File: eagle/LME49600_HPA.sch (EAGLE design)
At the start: 20 parts, among them IC1 OPA2134P

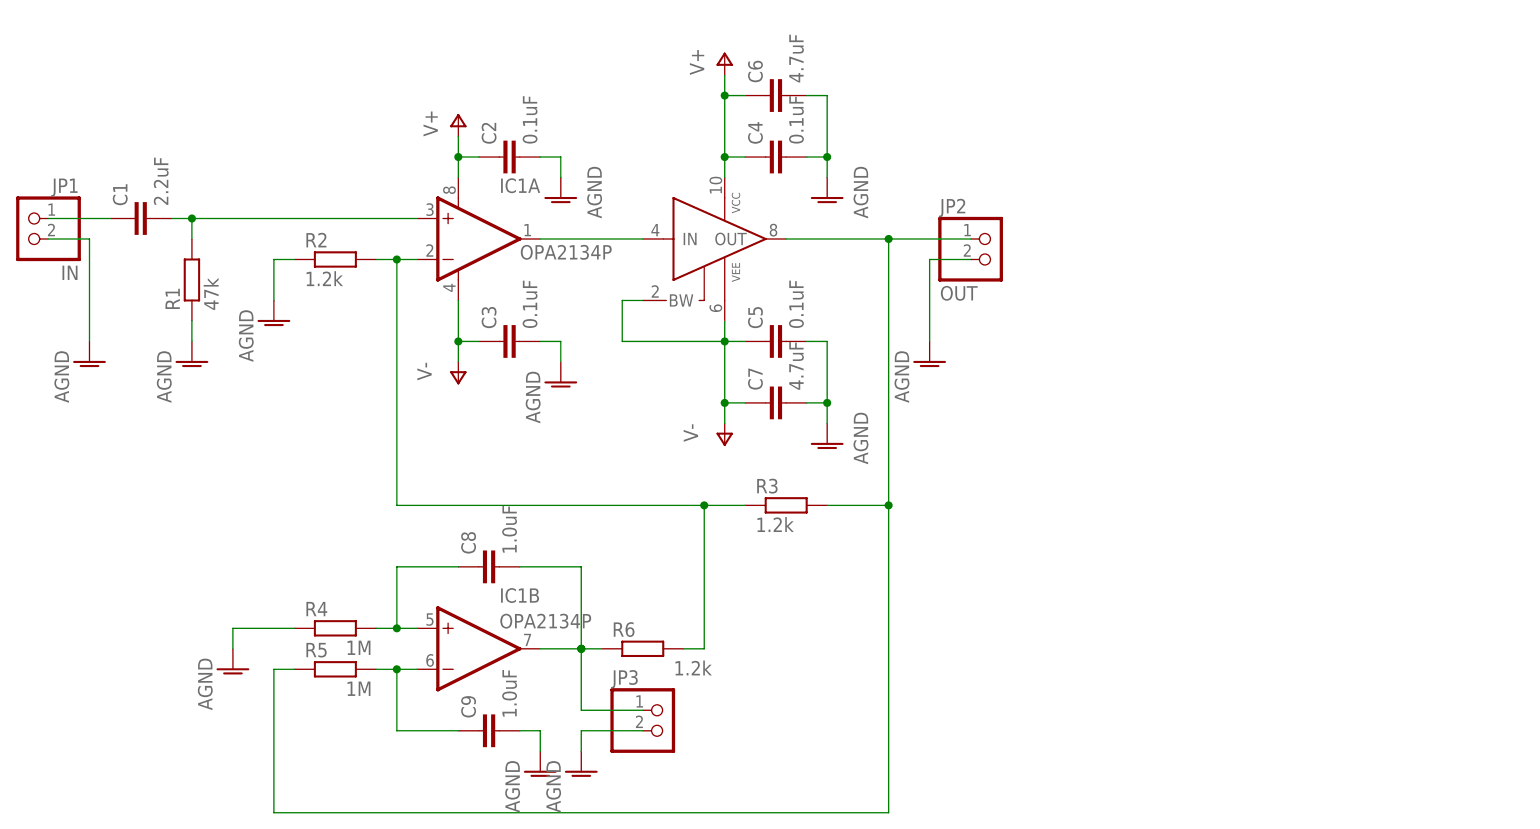
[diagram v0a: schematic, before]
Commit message: Add: Power Supply
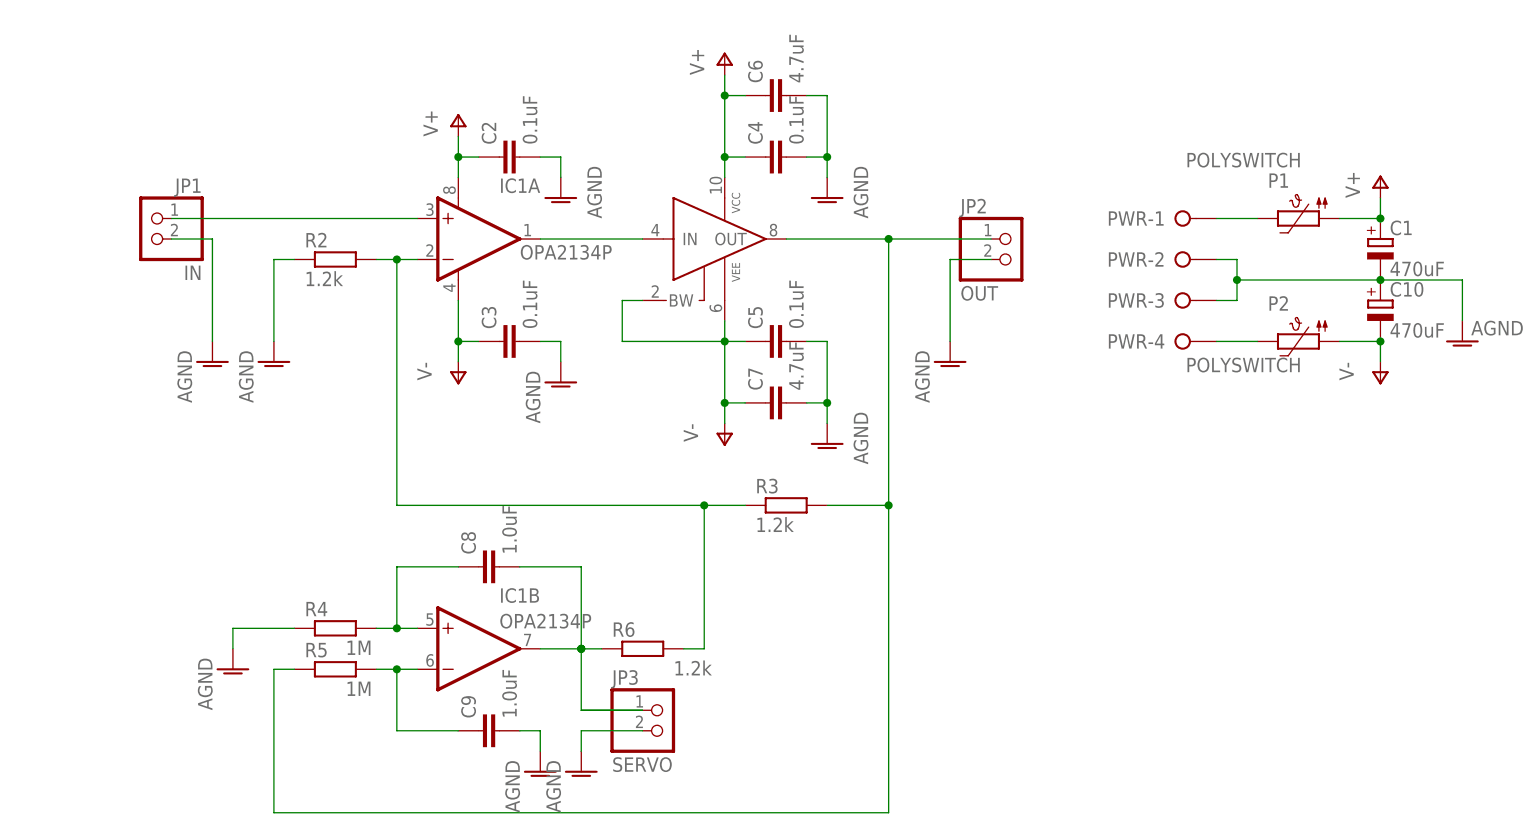
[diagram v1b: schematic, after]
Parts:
- removed R1: 47k, rcl:R-EU_0207/7
- added C10: 470uF, rcl:CPOL-EUE7.5-16
- added P1, P2: POLYSWITCH, mylib2:POLYSWITCH
- added PWR: (no value), con-wago-508:W237-04P
- C1: value 2.2uF -> 470uF; device rcl:C-EU050-075X075 -> rcl:CPOL-EUE7.5-16
- JP3: value (none) -> SERVO
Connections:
- removed net N$2: C1.2, IC1A.+IN, R1.2
- new net N$9: P2.2, PWR-4.KL
- new net P1: P1.2, PWR-1.KL
- net AGND: now also C1.-, C10.+, PWR-2.KL, PWR-3.KL; no longer R1.1
- net N$1: now also IC1A.+IN; no longer C1.1
- net V+: now also C1.+, P1.1
- net V-: now also C10.-, P2.1
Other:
- moved on the sheet: JP1, JP2
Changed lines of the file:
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@@
 <setting verticaltext="up"/>
 </settings>
-<grid distance="0.1" unitdist="inch" unit="inch" style="dots" multiple="1" display="yes" altdistance="0.01" altunitdist="inch" altunit="inch"/>
+<grid distance="0.1" unitdist="inch" unit="inch" style="lines" multiple="1" display="yes" altdistance="0.01" altunitdist="inch" altunit="inch"/>
 <layers>
 <layer number="1" name="Top" color="4" fill="1" visible="no" active="no"/>
@@
 <part name="JP1" library="pinhead" deviceset="PINHD-1X2" device="" value="IN"/>
 <part name="JP2" library="pinhead" deviceset="PINHD-1X2" device="" value="OUT"/>
-<part name="C1" library="rcl" deviceset="C-EU" device="050-075X075" value="2.2uF"/>
-<part name="R1" library="rcl" deviceset="R-EU_" device="0207/7" value="47k"/>
 <part name="AGND1" library="supply1" deviceset="AGND" device=""/>
-<part name="AGND2" library="supply1" deviceset="AGND" device=""/>
 <part name="IC1" library="burr-brown" deviceset="OPA2134" device="P"/>
 <part name="R2" library="rcl" deviceset="R-EU_" device="0207/7" value="1.2k"/>
@@
 <part name="AGND9" library="supply1" deviceset="AGND" device=""/>
 <part name="R6" library="rcl" deviceset="R-EU_" device="0207/7" value="1.2k"/>
-<part name="JP3" library="pinhead" deviceset="PINHD-1X2" device=""/>
+<part name="JP3" library="pinhead" deviceset="PINHD-1X2" device="" value="SERVO"/>
 <part name="AGND10" library="supply1" deviceset="AGND" device=""/>
 <part name="AGND11" library="supply1" deviceset="AGND" device=""/>
 <part name="P+2" library="supply1" deviceset="V+" device=""/>
 <part name="P-2" library="supply1" deviceset="V-" device=""/>
+<part name="PWR" library="con-wago-508" deviceset="W237-04P" device=""/>
+<part name="C1" library="rcl" deviceset="CPOL-EU" device="E7.5-16" value="470uF"/>
+<part name="C10" library="rcl" deviceset="CPOL-EU" device="E7.5-16" value="470uF"/>
+<part name="P1" library="mylib2" deviceset="POLYSWITCH" device=""/>
+<part name="P2" library="mylib2" deviceset="POLYSWITCH" device=""/>
+<part name="AGND2" library="supply1" deviceset="AGND" device=""/>
+<part name="P+3" library="supply1" deviceset="V+" device=""/>
+<part name="P-3" library="supply1" deviceset="V-" device=""/>
 </parts>
 <sheets>
@@
 </plain>
 <instances>
-<instance part="JP1" gate="G$1" x="33.02" y="83.82" rot="MR0"/>
-<instance part="JP2" gate="G$1" x="152.4" y="81.28"/>
-<instance part="C1" gate="G$1" x="45.72" y="86.36" rot="R90"/>
-<instance part="R1" gate="G$1" x="53.34" y="78.74" rot="R90"/>
-<instance part="AGND1" gate="VR1" x="40.64" y="68.58"/>
-<instance part="AGND2" gate="VR1" x="53.34" y="68.58"/>
+<instance part="JP1" gate="G$1" x="48.26" y="83.82" rot="MR0"/>
+<instance part="JP2" gate="G$1" x="154.94" y="81.28"/>
+<instance part="AGND1" gate="VR1" x="55.88" y="68.58"/>
 <instance part="IC1" gate="A" x="88.9" y="83.82" smashed="yes">
 <attribute name="NAME" x="91.44" y="89.535" size="1.778" layer="95"/>
@@
 </instance>
 <instance part="R2" gate="G$1" x="71.12" y="81.28"/>
-<instance part="AGND3" gate="VR1" x="63.5" y="73.66"/>
+<instance part="AGND3" gate="VR1" x="63.5" y="68.58"/>
 <instance part="C2" gate="G$1" x="91.44" y="93.98" rot="R90"/>
 <instance part="C3" gate="G$1" x="91.44" y="71.12" rot="R90"/>
@@
 <instance part="JP3" gate="G$1" x="111.76" y="22.86"/>
 <instance part="AGND10" gate="VR1" x="101.6" y="17.78"/>
-<instance part="AGND11" gate="VR1" x="144.78" y="68.58"/>
+<instance part="AGND11" gate="VR1" x="147.32" y="68.58"/>
 <instance part="P+2" gate="1" x="86.36" y="99.06"/>
 <instance part="P-2" gate="1" x="86.36" y="66.04"/>
+<instance part="PWR" gate="-1" x="175.26" y="86.36"/>
+<instance part="PWR" gate="-2" x="175.26" y="81.28"/>
+<instance part="PWR" gate="-3" x="175.26" y="76.2"/>
+<instance part="PWR" gate="-4" x="175.26" y="71.12"/>
+<instance part="C1" gate="G$1" x="200.66" y="83.82"/>
+<instance part="C10" gate="G$1" x="200.66" y="76.2"/>
+<instance part="P1" gate="G$1" x="190.5" y="86.36" smashed="yes">
+<attribute name="NAME" x="186.69" y="90.17" size="1.778" layer="95"/>
+<attribute name="VALUE" x="176.53" y="92.71" size="1.778" layer="96"/>
+</instance>
+<instance part="P2" gate="G$1" x="190.5" y="71.12" smashed="yes">
+<attribute name="NAME" x="186.69" y="74.93" size="1.778" layer="95"/>
+<attribute name="VALUE" x="176.53" y="67.31" size="1.778" layer="96"/>
+</instance>
+<instance part="AGND2" gate="VR1" x="210.82" y="71.12" smashed="yes">
+<attribute name="VALUE" x="218.44" y="73.66" size="1.778" layer="96" rot="R180"/>
+</instance>
+<instance part="P+3" gate="1" x="200.66" y="91.44"/>
+<instance part="P-3" gate="1" x="200.66" y="66.04"/>
 </instances>
 <busses>
 </busses>
 <nets>
-<net name="N$1" class="0">
-<segment>
-<pinref part="JP1" gate="G$1" pin="1"/>
-<pinref part="C1" gate="G$1" pin="1"/>
-<wire x1="35.56" y1="86.36" x2="43.18" y2="86.36" width="0.1524" layer="91"/>
-</segment>
-</net>
-<net name="N$2" class="0">
-<segment>
-<pinref part="C1" gate="G$1" pin="2"/>
-<pinref part="R1" gate="G$1" pin="2"/>
-<wire x1="50.8" y1="86.36" x2="53.34" y2="86.36" width="0.1524" layer="91"/>
-<wire x1="53.34" y1="86.36" x2="53.34" y2="83.82" width="0.1524" layer="91"/>
-<pinref part="IC1" gate="A" pin="+IN"/>
-<wire x1="81.28" y1="86.36" x2="53.34" y2="86.36" width="0.1524" layer="91"/>
-<junction x="53.34" y="86.36"/>
-</segment>
-</net>
 <net name="AGND" class="0">
 <segment>
 <pinref part="JP1" gate="G$1" pin="2"/>
 <pinref part="AGND1" gate="VR1" pin="AGND"/>
-<wire x1="35.56" y1="83.82" x2="40.64" y2="83.82" width="0.1524" layer="91"/>
-<wire x1="40.64" y1="83.82" x2="40.64" y2="71.12" width="0.1524" layer="91"/>
-</segment>
-<segment>
-<pinref part="AGND2" gate="VR1" pin="AGND"/>
-<pinref part="R1" gate="G$1" pin="1"/>
-<wire x1="53.34" y1="71.12" x2="53.34" y2="73.66" width="0.1524" layer="91"/>
+<wire x1="50.8" y1="83.82" x2="55.88" y2="83.82" width="0.1524" layer="91"/>
+<wire x1="55.88" y1="83.82" x2="55.88" y2="71.12" width="0.1524" layer="91"/>
 </segment>
 <segment>
 <pinref part="AGND3" gate="VR1" pin="AGND"/>
-<wire x1="63.5" y1="76.2" x2="63.5" y2="81.28" width="0.1524" layer="91"/>
+<wire x1="63.5" y1="71.12" x2="63.5" y2="81.28" width="0.1524" layer="91"/>
 <pinref part="R2" gate="G$1" pin="1"/>
 <wire x1="63.5" y1="81.28" x2="66.04" y2="81.28" width="0.1524" layer="91"/>
@@
 <segment>
 <pinref part="JP2" gate="G$1" pin="2"/>
-<wire x1="149.86" y1="81.28" x2="144.78" y2="81.28" width="0.1524" layer="91"/>
+<wire x1="152.4" y1="81.28" x2="147.32" y2="81.28" width="0.1524" layer="91"/>
 <pinref part="AGND11" gate="VR1" pin="AGND"/>
-<wire x1="144.78" y1="81.28" x2="144.78" y2="71.12" width="0.1524" layer="91"/>
+<wire x1="147.32" y1="81.28" x2="147.32" y2="71.12" width="0.1524" layer="91"/>
+</segment>
+<segment>
+<wire x1="101.6" y1="25.4" x2="109.22" y2="25.4" width="0.1524" layer="91"/>
+</segment>
+<segment>
+<pinref part="PWR" gate="-2" pin="KL"/>
+<wire x1="180.34" y1="81.28" x2="182.88" y2="81.28" width="0.1524" layer="91"/>
+<wire x1="182.88" y1="81.28" x2="182.88" y2="78.74" width="0.1524" layer="91"/>
+<pinref part="PWR" gate="-3" pin="KL"/>
+<wire x1="182.88" y1="78.74" x2="182.88" y2="76.2" width="0.1524" layer="91"/>
+<wire x1="182.88" y1="76.2" x2="180.34" y2="76.2" width="0.1524" layer="91"/>
+<pinref part="C1" gate="G$1" pin="-"/>
+<pinref part="C10" gate="G$1" pin="+"/>
+<wire x1="182.88" y1="78.74" x2="200.66" y2="78.74" width="0.1524" layer="91"/>
+<junction x="182.88" y="78.74"/>
+<junction x="200.66" y="78.74"/>
+<pinref part="AGND2" gate="VR1" pin="AGND"/>
+<wire x1="200.66" y1="78.74" x2="210.82" y2="78.74" width="0.1524" layer="91"/>
+<wire x1="210.82" y1="78.74" x2="210.82" y2="73.66" width="0.1524" layer="91"/>
 </segment>
 </net>
@@
 <junction x="86.36" y="71.12"/>
 </segment>
+<segment>
+<pinref part="P2" gate="G$1" pin="1"/>
+<pinref part="C10" gate="G$1" pin="-"/>
+<wire x1="195.58" y1="71.12" x2="200.66" y2="71.12" width="0.1524" layer="91"/>
+<pinref part="P-3" gate="1" pin="V-"/>
+<wire x1="200.66" y1="71.12" x2="200.66" y2="68.58" width="0.1524" layer="91"/>
+<junction x="200.66" y="71.12"/>
+</segment>
 </net>
 <net name="V+" class="0">
@@
 <wire x1="86.36" y1="96.52" x2="86.36" y2="93.98" width="0.1524" layer="91"/>
 <junction x="86.36" y="93.98"/>
+</segment>
+<segment>
+<pinref part="P1" gate="G$1" pin="1"/>
+<pinref part="C1" gate="G$1" pin="+"/>
+<wire x1="195.58" y1="86.36" x2="200.66" y2="86.36" width="0.1524" layer="91"/>
+<pinref part="P+3" gate="1" pin="V+"/>
+<wire x1="200.66" y1="88.9" x2="200.66" y2="86.36" width="0.1524" layer="91"/>
+<junction x="200.66" y="86.36"/>
 </segment>
 </net>
@@
 <pinref part="U$1" gate="G$1" pin="OUT"/>
 <wire x1="127" y1="83.82" x2="139.7" y2="83.82" width="0.1524" layer="91"/>
-<wire x1="139.7" y1="83.82" x2="149.86" y2="83.82" width="0.1524" layer="91"/>
+<wire x1="139.7" y1="83.82" x2="152.4" y2="83.82" width="0.1524" layer="91"/>
 <junction x="139.7" y="83.82"/>
 <wire x1="139.7" y1="83.82" x2="139.7" y2="50.8" width="0.1524" layer="91"/>
@@
 </segment>
 </net>
+<net name="N$1" class="0">
+<segment>
+<pinref part="IC1" gate="A" pin="+IN"/>
+<wire x1="50.8" y1="86.36" x2="81.28" y2="86.36" width="0.1524" layer="91"/>
+<pinref part="JP1" gate="G$1" pin="1"/>
+</segment>
+</net>
+<net name="P1" class="0">
+<segment>
+<pinref part="P1" gate="G$1" pin="2"/>
+<pinref part="PWR" gate="-1" pin="KL"/>
+<wire x1="185.42" y1="86.36" x2="180.34" y2="86.36" width="0.1524" layer="91"/>
+</segment>
+</net>
+<net name="N$9" class="0">
+<segment>
+<pinref part="P2" gate="G$1" pin="2"/>
+<pinref part="PWR" gate="-4" pin="KL"/>
+<wire x1="185.42" y1="71.12" x2="180.34" y2="71.12" width="0.1524" layer="91"/>
+</segment>
+</net>

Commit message: 2ch
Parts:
- added C11, C12, C13, C14: 0.1uF, rcl:C-EU075-042X103
- added C15, C16: 4.7uF, rcl:C-EU075-042X103
- added C17, C18: 1.0uF, rcl:C-EU050-050X075
- added IC2: OPA2134P, burr-brown:OPA2134P
- added JP4: IN, pinhead:PINHD-1X2
- added JP5: OUT, pinhead:PINHD-1X2
- added JP6: SERVO, pinhead:PINHD-1X2
- added R1, R10, R7: 1.2k, rcl:R-EU_0207/7
- added R8, R9: 1M, rcl:R-EU_0207/7
- added U$2: LME49600_BRD, mylib2:LME49600_BRD
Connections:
- new net N$10: C18.1, IC2B.-IN, R9.2
- new net N$12: C17.2, IC2B.OUT, JP6.1, R10.1
- new net N$13: JP5.1, R7.2, R9.1, U$2.OUT
- new net N$15: IC2A.+IN, JP4.1
- new net N$2: IC2A.-IN, R1.2, R10.2, R7.1
- new net N$4: IC2A.OUT, U$2.IN
- new net N$5: C17.1, IC2B.+IN, R8.2
- net AGND: now also C11.2, C12.2, C13.2, C14.2, C15.2, C16.2, C18.2, JP4.2, JP5.2, JP6.2, R1.1, R8.1
- net V+: now also C11.1, C13.1, C15.1, IC2A.V+, U$2.VCC
- net V-: now also C12.1, C14.1, C16.1, IC2A.V-, U$2.BW, U$2.VEE@1
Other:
- moved on the sheet: C1, C10, C2, C3, C4, C5, C6, C7, C8, C9, IC1A, IC1B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

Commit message: bug fix
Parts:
- C15, C16: value 4.7uF -> 1.0uF; device rcl:C-EU075-042X103 -> rcl:C-EU050-050X075
- C17, C18: value 1.0uF -> 4.7uF; device rcl:C-EU050-050X075 -> rcl:CPOL-EUE2-4
- C6, C7: device rcl:C-EU075-042X103 -> rcl:CPOL-EUE2-4
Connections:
- net N$9 renamed PW-
- net P1 renamed PW+
- removed net N$12 (its old number): C17.2, IC2B.OUT, JP6.1, R10.1
- new net N$9: C16.1, IC2B.+IN, R9.2
- net AGND: now also C17.-, C18.+, C6.-, C7.+; no longer C15.2, C18.2, C6.2, C7.2
- net N$10: now also C15.2, IC2B.OUT, JP6.1, R10.1; no longer C18.1, IC2B.-IN, R9.2
- net N$5: now also C15.1, IC2B.-IN; no longer C17.1, IC2B.+IN
- net N$6: now also IC1B.-IN; no longer IC1B.+IN
- net N$8: now also IC1B.+IN; no longer IC1B.-IN
- net V+: now also C17.+, C6.+; no longer C15.1, C6.1
- net V-: now also C18.-, C7.-; no longer C16.1, C7.1
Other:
- moved on the sheet: C1, C10, C11, C12, C13, C14, C15, C16, IC1B, IC2A, IC2B, JP4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

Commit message: bug fix
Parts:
- removed JP3, JP6: SERVO, pinhead:PINHD-1X2
- added C19: 4.7uF, rcl:CPOL-EUE2-4
- added C20: (no value), rcl:C-EU050-055X075
- added R11, R12: 1.2k, rcl:R-EU_0207/7
- C11: value 0.1uF -> (none); device rcl:C-EU075-042X103 -> rcl:C-EU050-055X075
- C15: value 1.0uF -> 0.1uF; device rcl:C-EU050-050X075 -> rcl:C-EU075-042X103
- C17: value 4.7uF -> 1.0uF; device rcl:CPOL-EUE2-4 -> rcl:C-EU050-050X075
- R10: value 1.2k -> 1M
- R8: value 1M -> 1.2k
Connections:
- removed net N$5 (its old number): C15.1, IC2B.-IN, R8.2
- new net N$15: C20.2, JP4.1
- new net N$16: C20.1, IC2A.+IN, R12.2
- new net N$4: IC2A.-IN, R11.2, R7.2, R8.1
- net AGND: now also C15.2, C17.2, C18.-, C19.+, R12.1, R7.1, R9.1; no longer C11.2, C16.2, C17.-, C18.+, JP3.2, JP6.2, R8.1
- net N$1: now also C11.2; no longer IC1A.+IN
- net N$10: now also C17.1, IC2B.+IN, R10.2; no longer C15.2, IC2B.OUT, JP6.1, R10.1
- net N$11: no longer JP3.1
- net N$12: now also C16.2, IC2B.OUT, R11.1; no longer JP5.1, R7.2, R9.1, U$2.OUT
- net N$13: now also JP5.1, R10.1, R8.2, U$2.OUT; no longer IC2A.+IN, JP4.1
- net N$2: now also C11.1, IC1A.+IN; no longer IC2A.-IN, R10.2, R7.1
- net N$9: now also IC2B.-IN; no longer IC2B.+IN
- net V+: now also C12.1, C14.1, C18.+; no longer C11.1, C13.1, C17.+
- net V-: now also C13.1, C15.1, C19.-; no longer C12.1, C14.1, C18.-
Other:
- note added: "R1, R12, C11, C22はピンソケットで実装"
- moved on the sheet: C1, C10, C11, C12, C13, C14, C15, C16, C18, C2, C3, C4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
